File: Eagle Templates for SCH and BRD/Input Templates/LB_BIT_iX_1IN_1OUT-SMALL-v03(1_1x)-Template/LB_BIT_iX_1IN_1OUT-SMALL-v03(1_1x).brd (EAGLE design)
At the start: 21.4 x 11.6 mm, 17 parts, among them U1 LV321SOT23-5, U2 LV321SOT23-5

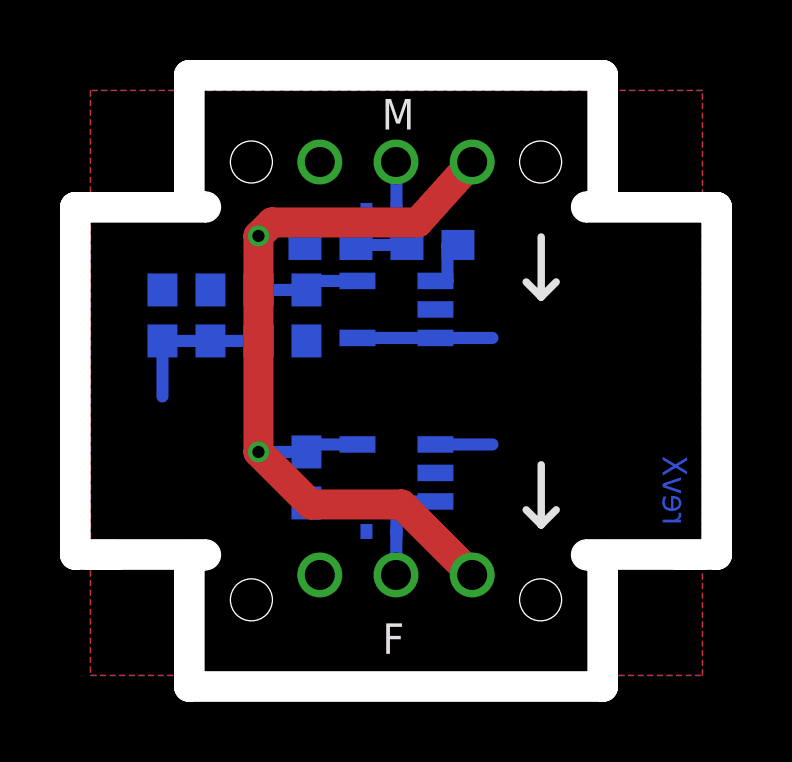
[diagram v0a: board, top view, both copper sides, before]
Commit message: added bitlab logo and made minor changes to board templates. Updated littlebits library.
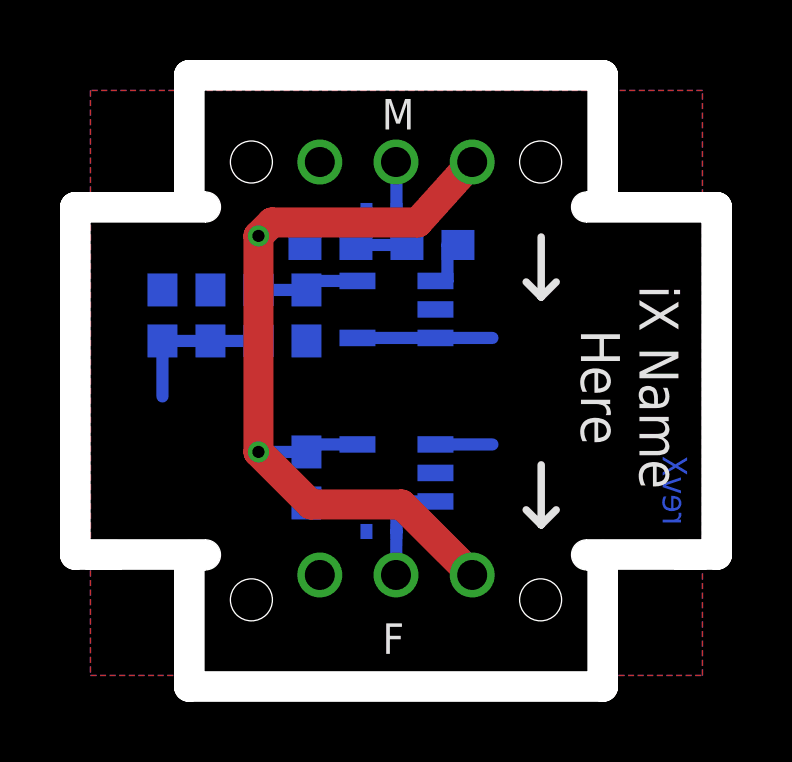
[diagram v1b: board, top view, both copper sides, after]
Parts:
- added U$5: (no value), LITTLEBITS:BITLAB-LOGO
- moved U$4 3.72 mm to (15.4, 9.90)
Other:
- board text added: "iX Name Here"
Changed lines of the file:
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@@
 <layer number="113" name="extra" color="10" fill="1" visible="yes" active="yes"/>
 <layer number="116" name="Patch_BOT" color="9" fill="4" visible="yes" active="yes"/>
+<layer number="118" name="Rect_Pads" color="7" fill="1" visible="no" active="yes"/>
 <layer number="121" name="_tsilk" color="7" fill="1" visible="yes" active="yes"/>
 <layer number="122" name="_bsilk" color="7" fill="1" visible="yes" active="yes"/>
@@
 <dimension x1="3.01" y1="4.61" x2="23.41" y2="4.61" x3="13.21" y3="-3.98" textsize="1.778" layer="113"/>
 <text x="22.1" y="5.1" size="0.8128" layer="16" font="vector" ratio="12" rot="MR90">revX</text>
+<text x="21" y="9.7" size="1.3" layer="21" font="vector" rot="SR270" align="center">iX Name
+Here</text>
 </plain>
 <attributes>
@@
 <element name="U$2" library="LITTLEBITS" package="OSHWCREDIT" value="OSHWCREDIT" x="-92.24" y="-64.31"/>
 <element name="U$3" library="LITTLEBITS" package="FABDWG01-OHW" value="FRAME-LETTER" x="0" y="0"/>
-<element name="U$4" library="ohw-logo" package="OSHW_FILLX150_NOTEXT" value="" x="19.1" y="10.3" rot="MR90"/>
+<element name="U$4" library="ohw-logo" package="OSHW_FILLX150_NOTEXT" value="" x="15.4" y="9.9" rot="MR90"/>
+<element name="U$5" library="LITTLEBITS" package="BITLAB-LOGO" value="" x="19.8" y="14" rot="R270"/>
 </elements>
 <signals>

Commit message: Updated templates
- Added ferrite beads
- Moved text and annotations off of Nets layer
- Minor layout changes
- Removed I/O/W prefix from reference designators
- Removed output stage components from output bits
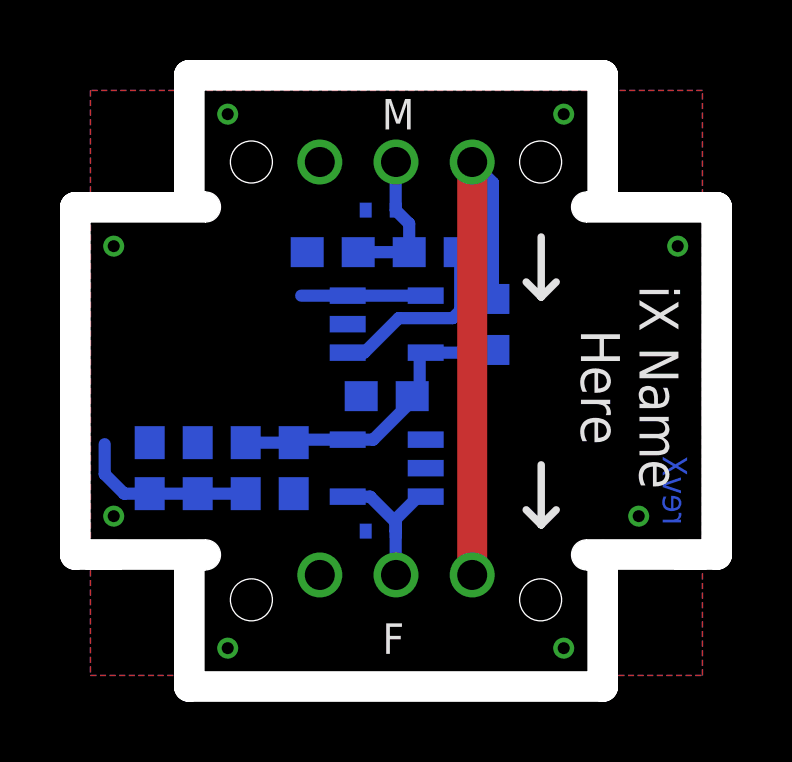
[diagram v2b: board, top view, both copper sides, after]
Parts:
- removed I?C1: 0.1uF, LITTLEBITS:CAP-0603
- removed I?C2: 10uF, LITTLEBITS:CAP-0603
- removed I?C3: 1.0uF, LITTLEBITS:CAP-0603
- removed I?R1: 1meg, LITTLEBITS:RES-0603
- removed I?R2: 10K, LITTLEBITS:RES-0603
- removed I?R3, I?R4: 3K3, LITTLEBITS:RES-0603
- removed I?TVS1, I?TVS2: ESD9B5.0ST5G, LITTLEBITS:SOD-923
- added C1: 0.1uF, LITTLEBITS:CAP-0603
- added C2: 10uF, LITTLEBITS:CAP-0603
- added C3: 1.0uF, LITTLEBITS:CAP-0603
- added FB1: FERRITE-BEAD0603, LITTLEBITS:R0603
- added R1: 1meg, LITTLEBITS:RES-0603
- added R2: 10K, LITTLEBITS:RES-0603
- added R3, R4: 3K3, LITTLEBITS:RES-0603
- added TVS1, TVS2: ESD9B5.0ST5G, LITTLEBITS:SOD-923
- moved U1 0.59 mm to (12.9, 11.8), turned to 90 degrees
- moved U2 0.36 mm to (12.9, 7.00)
- renumbered I?BSF to BSF1, I?BSM to BSM1
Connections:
- new net LB_VCC: BSF1.VCC, BSM1.VCC1, FB1.2
- net GND: now also C1.2, C2.2, C3.1, R1.1, R4.1, TVS1.1, TVS2.1; no longer I?C1.2, I?C2.2, I?C3.1, I?R1.1, I?R4.1, I?TVS1.1, I?TVS2.1
- net N$4: now also R2.1; no longer I?R2.1
- net SIG_IN: now also R1.2, R2.2, TVS1.2; no longer I?R1.2, I?R2.2, I?TVS1.2
- net SIG_OUT: now also TVS2.2; no longer I?TVS2.2
- net VCC: now also C1.1, C3.2, FB1.1, R3.2; no longer BSF1.VCC, BSM1.VCC1, I?C1.1, I?C3.2, I?R3.2
- net VREF: now also C2.1, R3.1, R4.2; no longer I?C2.1, I?R3.1, I?R4.2
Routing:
- net VCC: track 33.4 -> 10.6 mm, vias 2 -> 0
- net LB_VCC: track 0.00 -> 18.6 mm
- net N$4: track 1.95 -> 6.28 mm
- net N$3: track 2.00 -> 0.00 mm
- net VREF: track 5.10 -> 5.97 mm
